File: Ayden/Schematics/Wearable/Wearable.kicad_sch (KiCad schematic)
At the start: 5 parts

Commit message: Included TPL5111 timer in schematic
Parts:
- added U?: Adafruit_TPL5111_Breakout, Package_TO_SOT_SMD:SOT-23-6, symbol Timer:TPL5111
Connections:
- net at BT?.1 (+), U?.1 (Vin): now also U?.1 (VDD)
- net at A?.4 (GND), BT?.2 (-), U?.1 (GND)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: now also U?.2 (GND)
- net at U?.4 (En): now also U?.6 (EN/ONE_SHOT)
- net at A?.11 (D8): now also U?.4 (DONE)
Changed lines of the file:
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@@
   (junction (at 153.67 81.28) (diameter 0) (color 0 0 0 0)
   )
+  (junction (at 72.39 78.74) (diameter 0) (color 0 0 0 0)
+  )
+  (junction (at 62.23 62.23) (diameter 0) (color 0 0 0 0)
+  )
   (junction (at 74.93 78.74) (diameter 0) (color 0 0 0 0)
   )
@@
   (junction (at 151.13 138.43) (diameter 0) (color 0 0 0 0)
   )
+  (wire (pts (xy 127 50.8) (xy 127 72.39))
+    (stroke (width 0) (type default) (color 0 0 0 0))
+  )
   (wire (pts (xy 119.38 104.14) (xy 132.08 104.14))
     (stroke (width 0) (type default) (color 0 0 0 0))
@@
     (stroke (width 0) (type default) (color 0 0 0 0))
   )
+  (wire (pts (xy 96.52 38.1) (xy 96.52 62.23))
+    (stroke (width 0) (type default) (color 0 0 0 0))
+  )
+  (wire (pts (xy 134.62 54.61) (xy 139.7 54.61))
+    (stroke (width 0) (type default) (color 0 0 0 0))
+  )
   (wire (pts (xy 124.46 114.3) (xy 119.38 114.3))
     (stroke (width 0) (type default) (color 0 0 0 0))
@@
     (stroke (width 0) (type default) (color 0 0 0 0))
   )
+  (wire (pts (xy 72.39 78.74) (xy 74.93 78.74))
+    (stroke (width 0) (type default) (color 0 0 0 0))
+  )
   (wire (pts (xy 62.23 62.23) (xy 72.39 62.23))
     (stroke (width 0) (type default) (color 0 0 0 0))
   )
+  (wire (pts (xy 139.7 54.61) (xy 139.7 40.64))
+    (stroke (width 0) (type default) (color 0 0 0 0))
+  )
   (wire (pts (xy 195.58 88.9) (xy 168.91 88.9))
     (stroke (width 0) (type default) (color 0 0 0 0))
@@
     (stroke (width 0) (type default) (color 0 0 0 0))
   )
+  (wire (pts (xy 111.76 38.1) (xy 96.52 38.1))
+    (stroke (width 0) (type default) (color 0 0 0 0))
+  )
   (wire (pts (xy 127 123.19) (xy 138.43 123.19))
     (stroke (width 0) (type default) (color 0 0 0 0))
@@
     (stroke (width 0) (type default) (color 0 0 0 0))
   )
+  (wire (pts (xy 96.52 62.23) (xy 80.01 62.23))
+    (stroke (width 0) (type default) (color 0 0 0 0))
+  )
   (wire (pts (xy 168.91 120.65) (xy 163.83 120.65))
     (stroke (width 0) (type default) (color 0 0 0 0))
@@
     (stroke (width 0) (type default) (color 0 0 0 0))
   )
+  (wire (pts (xy 127 72.39) (xy 72.39 72.39))
+    (stroke (width 0) (type default) (color 0 0 0 0))
+  )
   (wire (pts (xy 124.46 125.73) (xy 138.43 125.73))
     (stroke (width 0) (type default) (color 0 0 0 0))
@@
     (stroke (width 0) (type default) (color 0 0 0 0))
   )
+  (wire (pts (xy 62.23 27.94) (xy 62.23 62.23))
+    (stroke (width 0) (type default) (color 0 0 0 0))
+  )
+  (wire (pts (xy 127 27.94) (xy 62.23 27.94))
+    (stroke (width 0) (type default) (color 0 0 0 0))
+  )
   (wire (pts (xy 73.66 138.43) (xy 106.68 138.43))
     (stroke (width 0) (type default) (color 0 0 0 0))
@@
     (stroke (width 0) (type default) (color 0 0 0 0))
   )
+  (wire (pts (xy 134.62 115.57) (xy 138.43 115.57))
+    (stroke (width 0) (type default) (color 0 0 0 0))
+  )
   (wire (pts (xy 168.91 88.9) (xy 168.91 120.65))
     (stroke (width 0) (type default) (color 0 0 0 0))
   )
+  (wire (pts (xy 134.62 54.61) (xy 134.62 115.57))
+    (stroke (width 0) (type default) (color 0 0 0 0))
+  )
   (wire (pts (xy 132.08 118.11) (xy 132.08 104.14))
     (stroke (width 0) (type default) (color 0 0 0 0))
@@
     (stroke (width 0) (type default) (color 0 0 0 0))
   )
+  (wire (pts (xy 72.39 72.39) (xy 72.39 78.74))
+    (stroke (width 0) (type default) (color 0 0 0 0))
+  )
   (wire (pts (xy 77.47 62.23) (xy 77.47 77.47))
     (stroke (width 0) (type default) (color 0 0 0 0))
@@
     (stroke (width 0) (type default) (color 0 0 0 0))
   )
-  (wire (pts (xy 69.85 78.74) (xy 74.93 78.74))
+  (wire (pts (xy 69.85 78.74) (xy 72.39 78.74))
     (stroke (width 0) (type default) (color 0 0 0 0))
   )
@@
     (pin "8")
     (pin "9")
+  )
+  (symbol (lib_id "Timer:TPL5111") (at 127 40.64 0) (unit 1)
+    (in_bom yes) (on_board yes) (fields_autoplaced)
+    (property "Reference" "U?" (id 0) (at 129.0194 25.4 0)
+      (effects (font (size 1.27 1.27)) (justify left))
+    )
+    (property "Value" "Adafruit_TPL5111_Breakout" (id 1) (at 129.0194 27.94 0)
+      (effects (font (size 1.27 1.27)) (justify left))
+    )
+    (property "Footprint" "Package_TO_SOT_SMD:SOT-23-6" (id 2) (at 127 40.64 0)
+      (effects (font (size 1.27 1.27)) hide)
+    )
+    (property "Datasheet" "http://www.ti.com/lit/ds/symlink/tpl5111.pdf" (id 3) (at 85.09 36.83 0)
+      (effects (font (size 1.27 1.27)) hide)
+    )
+    (pin "1")
+    (pin "2")
+    (pin "3")
+    (pin "4")
+    (pin "6")
   )
   (symbol (lib_id "Device:Battery_Cell") (at 67.31 78.74 90) (unit 1)
@@
       (reference "U?") (unit 1) (value "SEN0344") (footprint "")
     )
+    (path "/3d05921e-0db9-4f91-ad86-5016e423f983"
+      (reference "U?") (unit 1) (value "Adafruit_TPL5111_Breakout") (footprint "Package_TO_SOT_SMD:SOT-23-6")
+    )
     (path "/ff491504-4ea3-4688-8a78-809549125a47"

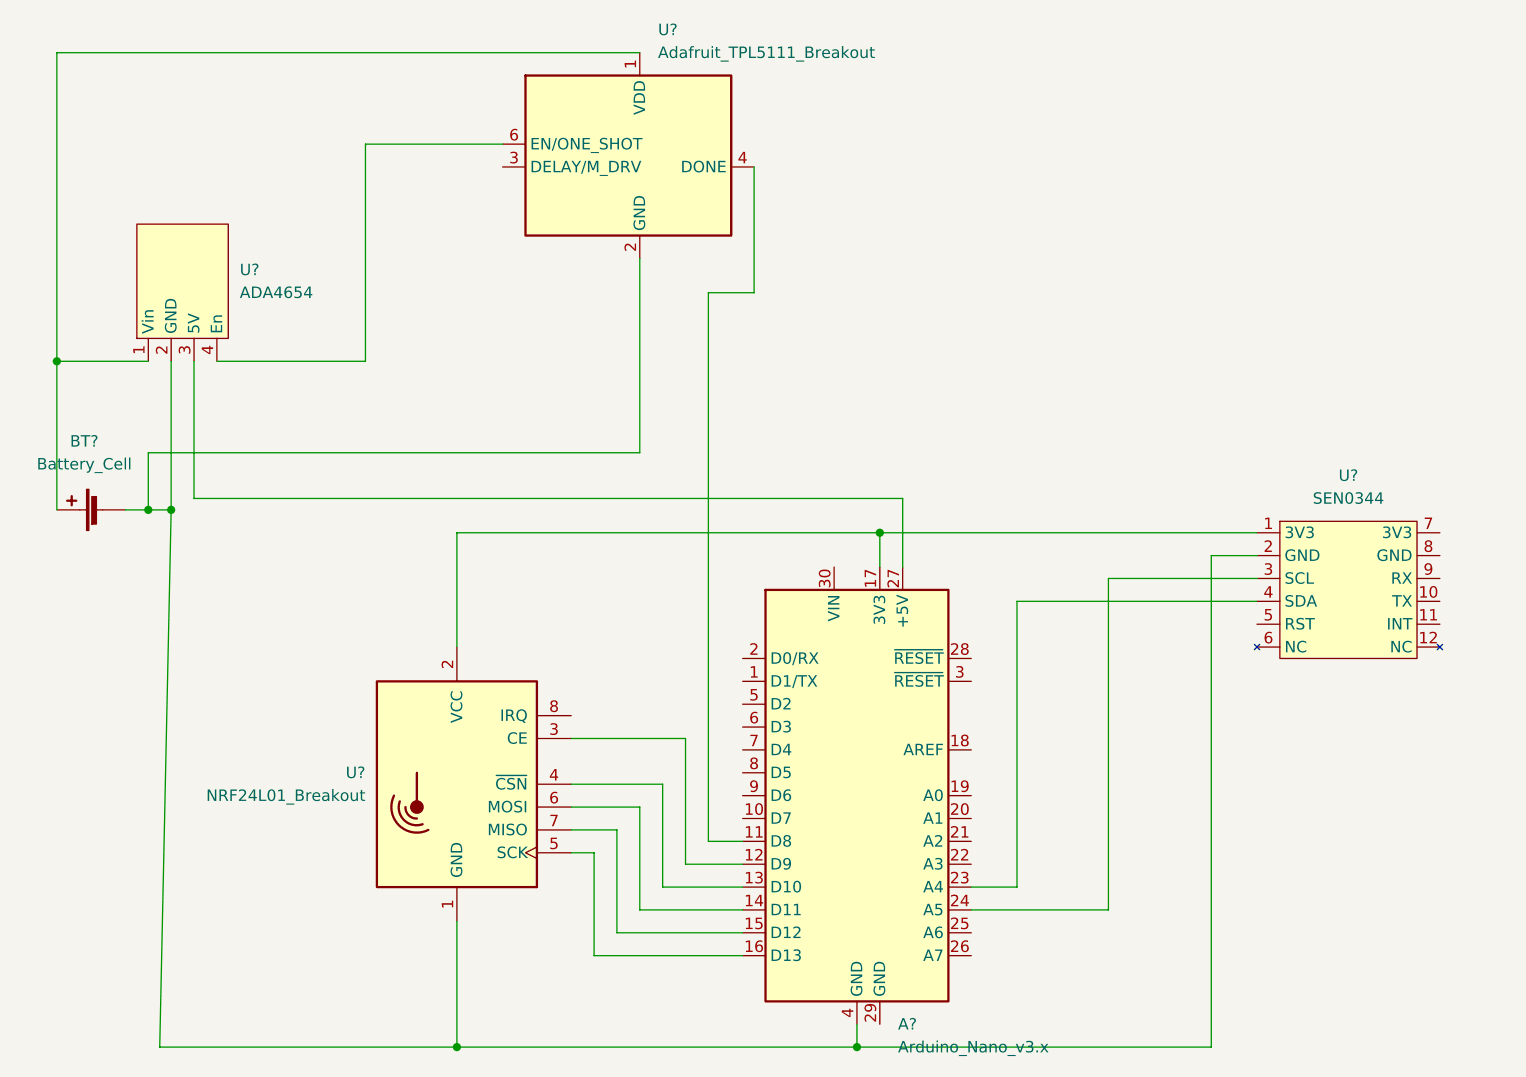
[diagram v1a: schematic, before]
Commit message: Update schematic to reflect true construction of circuit
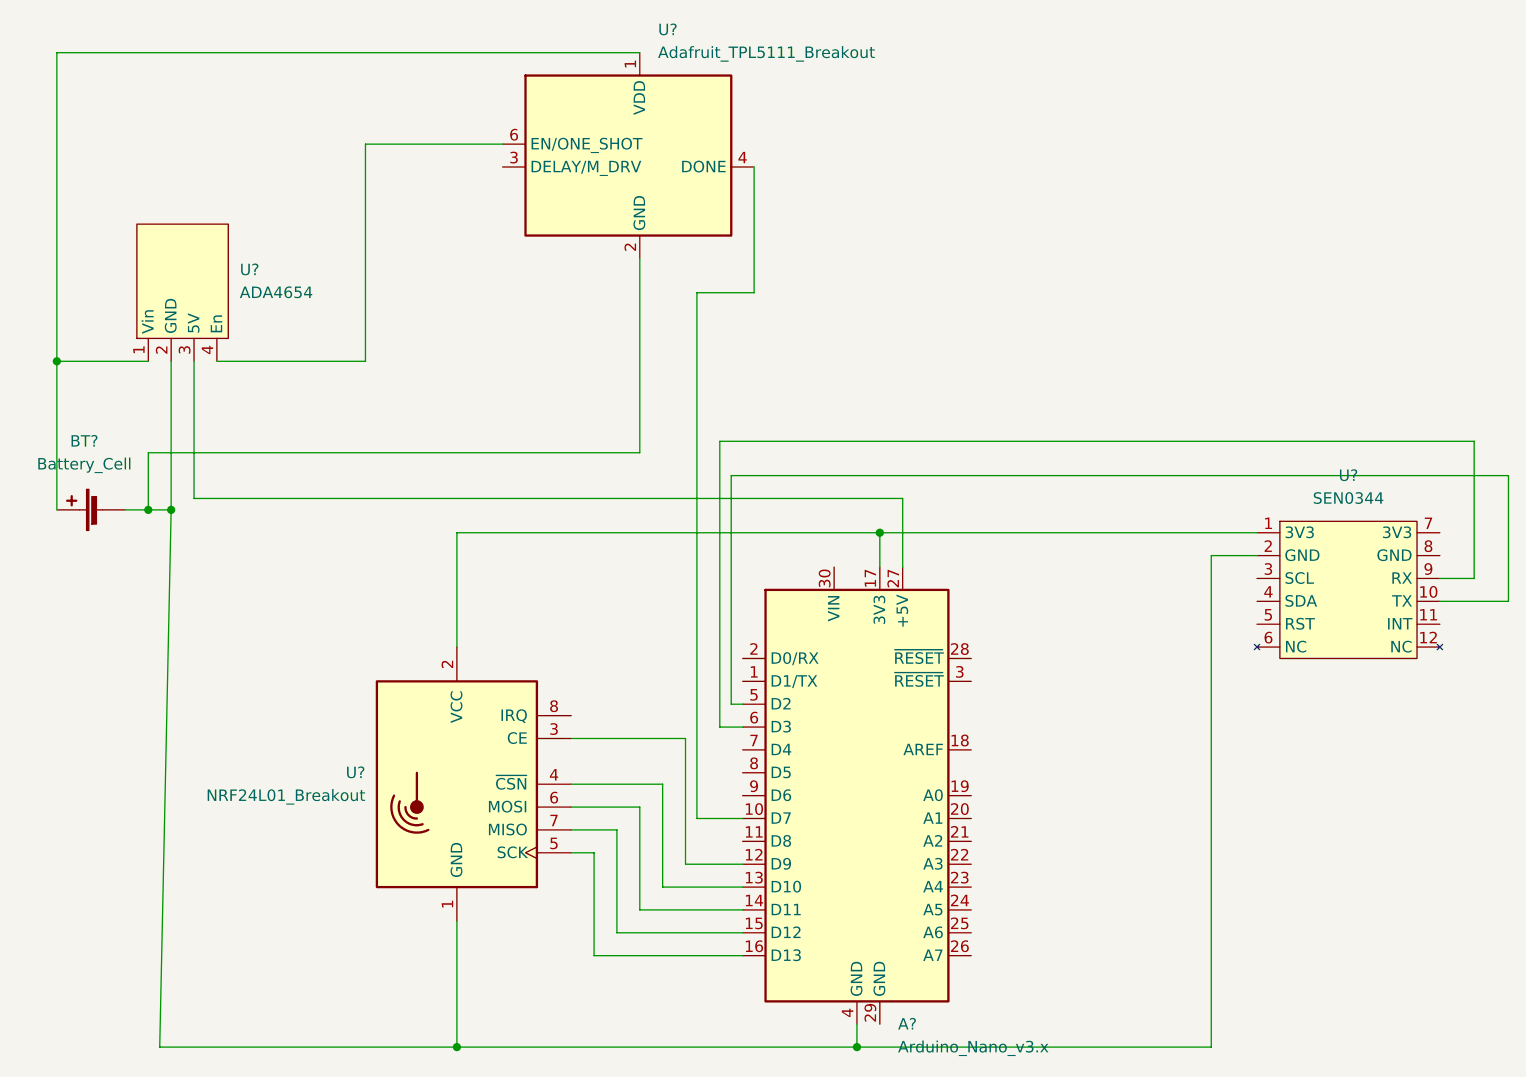
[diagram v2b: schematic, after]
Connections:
- net at U?.10 (TX): now also A?.5 (D2)
- net at U?.3 (SCL): no longer A?.24 (A5)
- net at U?.4 (SDA): no longer A?.23 (A4)
- net at U?.9 (RX): now also A?.6 (D3)
- net at U?.4 (DONE): now also A?.10 (D7); no longer A?.11 (D8)

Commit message: Organized schematic for project demo
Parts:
- A1: renamed from A?; value Arduino_Nano_v3.x -> Arduino_Nano
- U?: value ADA4654 -> ADA4654_Boost_Conv
- U?: value SEN0344 -> SEN0344_Pulse_SpO2
- U?: value Adafruit_TPL5111_Breakout -> Adafruit_TPL5111_Timer
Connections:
- net at A1.4 (GND), BT?.2 (-), U?.1 (GND)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: now also U?.8 (GND); no longer U?.2 (GND)
